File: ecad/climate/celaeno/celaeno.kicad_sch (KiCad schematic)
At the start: 9 parts, among them J1 MCV 1,5/ 2-G-3,5, J10 2.10mm ID, 5.5mm OD, J2 MCV 1,5/ 2-G-3,5, J3 5566-02A, J5 47053-1000, J6 47053-1000, J7 2.10mm ID, 5.5mm OD, J8 6410-02A, J9 6410-02A

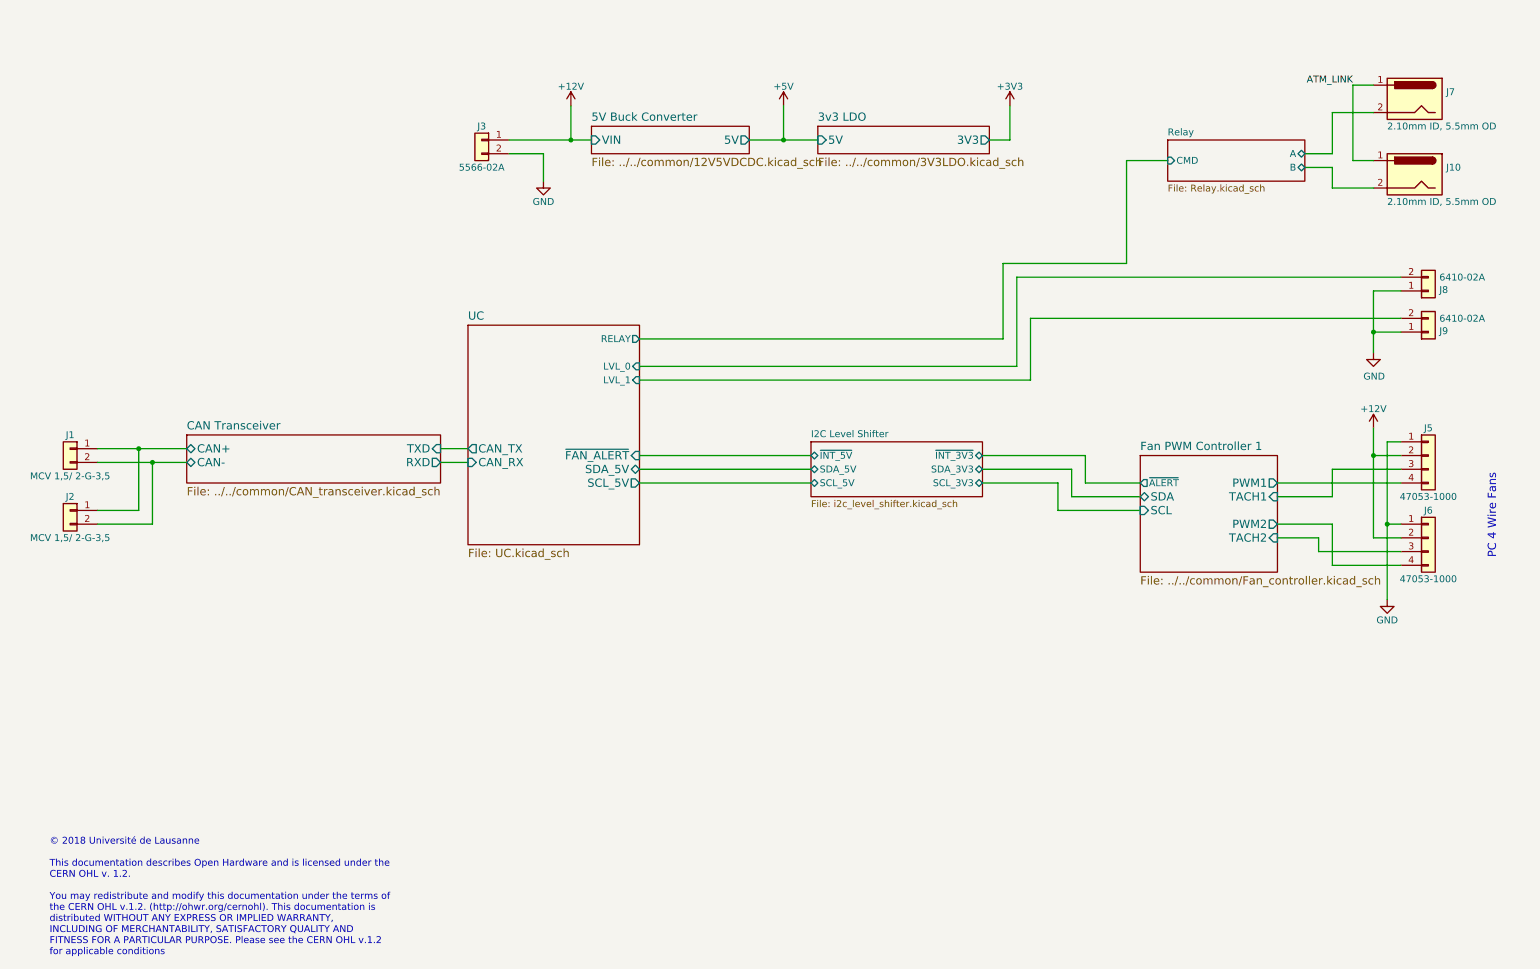
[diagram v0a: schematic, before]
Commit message: [WIP] Updating Celaeno to new connector and SSR
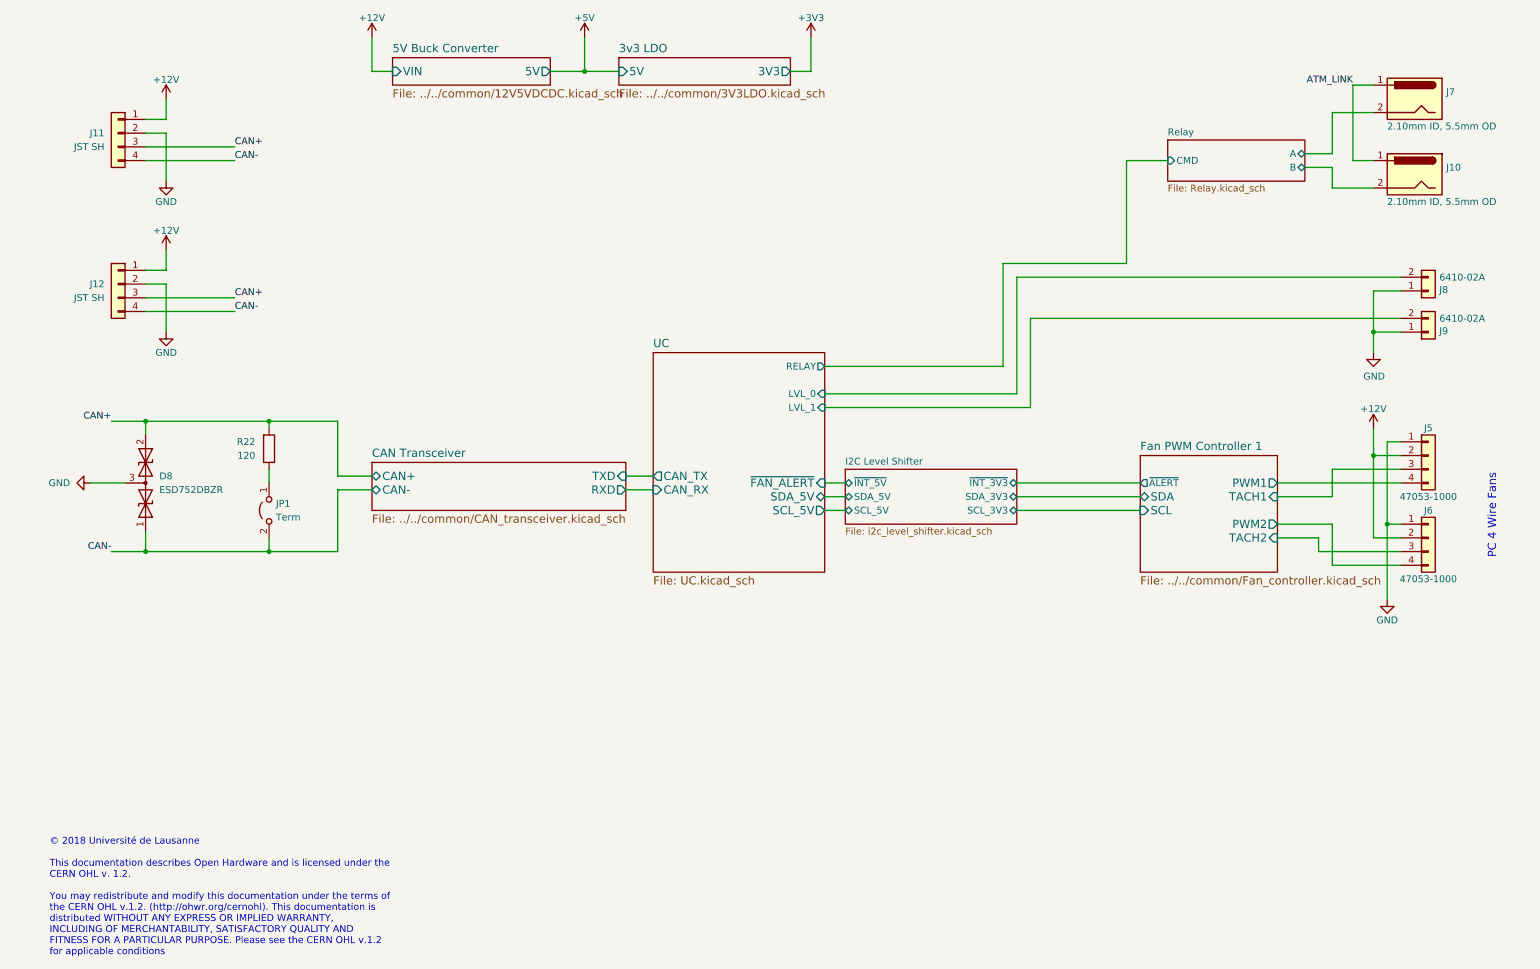
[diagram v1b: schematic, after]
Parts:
- removed J1, J2: MCV 1,5/ 2-G-3,5, Connector_Phoenix_MC:PhoenixContact_MCV_1,5_2-G-3.5_1x02_P3.50mm_Vertical, symbol Connector_Generic:Conn_01x02
- removed J3: 5566-02A, Connector_Molex:Molex_Mini-Fit_Jr_5566-02A_2x01_P4.20mm_Vertical, symbol Connector_Generic:Conn_01x02
- added D8: ESD752DBZR, Package_TO_SOT_SMD:SOT-23, symbol Device:D_TVS_Dual_AAC
- added J11, J12: JST SH, FORT:JST_PH_B4B-PH-SM4-TB_1x04-1MP_P2.00mm_Vertical, symbol Connector_Generic:Conn_01x04
- added JP1: Term, Connector_PinHeader_2.54mm:PinHeader_1x02_P2.54mm_Vertical, symbol Jumper:Jumper_2_Open
- added R22: 120, Resistor_SMD:R_0603_1608Metric, symbol Device:R
- J8, J9: footprint Connector_Molex:Molex_KK-254_AE-6410-02A_1x02_P2.54mm_Vertical -> Connector_JST:JST_PH_B2B-PH-SM4-TB_1x02-1MP_P2.00mm_Vertical
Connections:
- net +12V: now also J11.1 (Pin_1), J12.1 (Pin_1)
- net GND: now also D8.3 (common), J11.2 (Pin_2), J12.2 (Pin_2)
- new net: JP1.1 (A), R22.1
- new net CAN+: D8.2 (A2), J11.3 (Pin_3), J12.3 (Pin_3), R22.2
- new net CAN-: D8.1 (A1), J11.4 (Pin_4), J12.4 (Pin_4), JP1.2 (B)

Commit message: Updates Celaeno to new connector
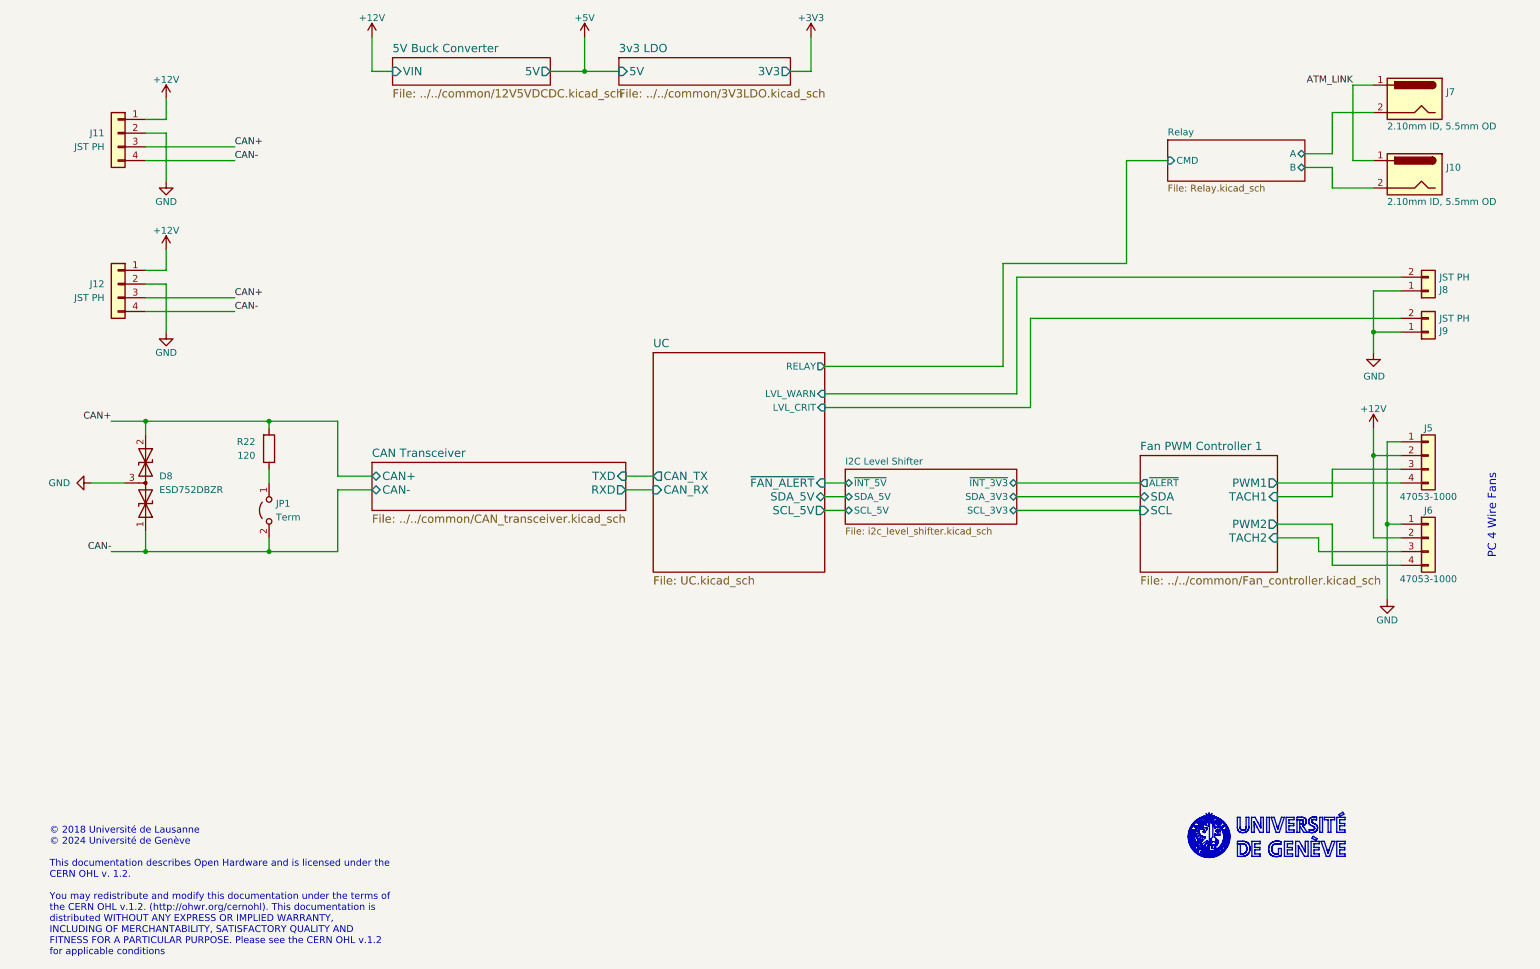
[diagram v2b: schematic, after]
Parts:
- J11, J12: value JST SH -> JST PH
- J8, J9: value 6410-02A -> JST PH
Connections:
- net UC/LVL_0 renamed UC/LVL_WARN
- net UC/LVL_1 renamed UC/LVL_CRIT
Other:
- sheet UC ports: added LVL_CRIT, LVL_WARN; removed LVL_0, LVL_1
- note added: "© 2018 Université de Lausanne © 2024 Université de Genève This documentation describes Open Hardware and is licensed under the CERN OHL v. 1.2. You may redistribute and modify this documentation under the terms of the CERN OHL v.1.2. (http://ohwr.org/cernohl). This documentation is distributed WITHOUT ANY EXPRESS OR IMPLIED WARRANTY, INCLUDING OF MERCHANTABILITY, SATISFACTORY QUALITY AND FITNESS 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"
- note removed: "© 2018 Université de Lausanne This documentation describes Open Hardware and is licensed under the CERN OHL v. 1.2. You may redistribute and modify this documentation under the terms of the CERN OHL v.1.2. (http://ohwr.org/cernohl). This documentation is distributed WITHOUT ANY EXPRESS OR IMPLIED WARRANTY, INCLUDING OF MERCHANTABILITY, SATISFACTORY QUALITY AND FITNESS FOR A PARTICULAR PURPOSE. Pl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"

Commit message: Updates Celaeno for production
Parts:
- D8: value ESD752DBZR -> CDSOT23-T24CAN; MPN (none) -> CDSOT23-T24CAN
- J10, J7: MPN (none) -> CUI_PJ-037B
- J11, J12: MPN B4B-PH-SM4 -> B4B-PH-SM4-TB
- J5, J6: MPN (none) -> 47053-1000
- J8, J9: MPN (none) -> B2B-PH-SM4-TB
- JP1: MPN (none) -> GPHA-1X02
- R22: MPN (none) -> GPR0603120R
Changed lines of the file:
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@@
 		)
 	)
+	(polyline
+		(pts
+			(xy 234.9055 173.9481) (xy 234.9055 173.9481)
+		)
+		(stroke
+			(width -0.0001)
+			(type solid)
+		)
+	)
 	(wire
 		(pts
@@
 	(polyline
 		(pts
-			(xy 234.9055 173.9481) (xy 234.9055 173.9481)
-		)
-		(stroke
-			(width -0.0001)
-			(type solid)
-		)
-		(fill
-			(type color)
-			(color 132 0 0 1)
-		)
-	)
-	(polyline
-		(pts
 			(xy 253.8033 176.0115) (xy 252.8249 176.0115) (xy 252.8249 176.6967) (xy 253.7536 176.6967) (xy 253.7536 177.1341)
 			(xy 252.8249 177.1341) (xy 252.8249 177.8894) (xy 253.8033 177.8894) (xy 253.8033 178.3476) (xy 252.2884 178.3476)
@@
 			)
 		)
-		(property "MPN" ""
+		(property "MPN" "47053-1000"
 			(at 269.24 104.14 0)
 			(effects
@@
 			)
 		)
-		(property "MPN" ""
+		(property "MPN" "47053-1000"
 			(at 269.24 119.38 0)
 			(effects
@@
 			)
 		)
-		(property "MPN" ""
+		(property "MPN" "B2B-PH-SM4-TB"
 			(at 269.24 73.66 0)
 			(effects
@@
 			)
 		)
-		(property "MPN" ""
+		(property "MPN" "CUI_PJ-037B"
 			(at 266.7 38.1 0)
 			(effects
@@
 			)
 		)
-		(property "MPN" ""
+		(property "MPN" "CUI_PJ-037B"
 			(at 266.7 52.07 0)
 			(effects
@@
 			)
 		)
-		(property "MPN" ""
+		(property "MPN" "B2B-PH-SM4-TB"
 			(at 269.24 81.28 0)
 			(effects
@@
 			)
 		)
-		(property "MPN" "B4B-PH-SM4"
+		(property "MPN" "B4B-PH-SM4-TB"
 			(at 26.67 44.45 0)
 			(effects
@@
 			)
 		)
+		(property "MPN" "GPHA-1X02"
+			(at 54.61 114.3 0)
+			(effects
+				(font
+					(size 1.27 1.27)
+				)
+				(hide yes)
+			)
+		)
 		(pin "2"
 		)
@@
 			)
 		)
-		(property "Value" "ESD752DBZR"
+		(property "Value" "CDSOT23-T24CAN"
 			(at 34.29 110.4899 90)
 			(effects
@@
 			)
 		)
+		(property "MPN" "CDSOT23-T24CAN"
+			(at 31.75 109.22 0)
+			(effects
+				(font
+					(size 1.27 1.27)
+				)
+				(hide yes)
+			)
+		)
 		(pin "1"
 		)
@@
 			)
 		)
-		(property "MPN" "B4B-PH-SM4"
+		(property "MPN" "B4B-PH-SM4-TB"
 			(at 26.67 72.39 0)
 			(effects
@@
 			(at 54.61 102.87 0)
 			(effects
+				(font
+					(size 1.27 1.27)
+				)
+				(hide yes)
+			)
+		)
+		(property "MPN" "GPR0603120R"
+			(at 54.61 102.87 0)
+			(effects

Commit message: Updates PCBs
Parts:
- J8, J9: footprint Connector_JST:JST_PH_B2B-PH-SM4-TB_1x02-1MP_P2.00mm_Vertical -> FORT:JST_PH_B2B-PH-SM4-TB_1x02-1MP_P2.00mm_Vertical
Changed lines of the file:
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@@
 			)
 		)
-		(property "Footprint" "Connector_JST:JST_PH_B2B-PH-SM4-TB_1x02-1MP_P2.00mm_Vertical"
+		(property "Footprint" "FORT:JST_PH_B2B-PH-SM4-TB_1x02-1MP_P2.00mm_Vertical"
 			(at 269.24 73.66 0)
 			(effects
@@
 			)
 		)
-		(property "Footprint" "Connector_JST:JST_PH_B2B-PH-SM4-TB_1x02-1MP_P2.00mm_Vertical"
+		(property "Footprint" "FORT:JST_PH_B2B-PH-SM4-TB_1x02-1MP_P2.00mm_Vertical"
 			(at 269.24 81.28 0)
 			(effects
